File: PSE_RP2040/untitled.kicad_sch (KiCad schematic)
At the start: 28 parts, among them J5 Screw_Terminal_01x02, U7 TPS2375-1, U8 LMR16006YQ

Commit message: modifiche lezione
usb mini,
check s1b
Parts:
- D6: value (none) -> D_Schottky; footprint (none) -> Diode_SMD:D_SMA
- R38, R39: footprint (none) -> Resistor_SMD:R_0603_1608Metric
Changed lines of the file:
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@@
     (property "Reference" "R39" (id 0) (at 102.87 57.15 90))
     (property "Value" "0R NF" (id 1) (at 102.87 59.69 90))
-    (property "Footprint" "" (id 2) (at 102.87 65.278 90)
+    (property "Footprint" "Resistor_SMD:R_0603_1608Metric" (id 2) (at 102.87 65.278 90)
       (effects (font (size 1.27 1.27)) hide)
     )
@@
     (property "Reference" "R38" (id 0) (at 63.5 125.73 90))
     (property "Value" "0R NF" (id 1) (at 63.5 128.27 90))
-    (property "Footprint" "" (id 2) (at 63.5 133.858 90)
+    (property "Footprint" "Resistor_SMD:R_0603_1608Metric" (id 2) (at 63.5 133.858 90)
       (effects (font (size 1.27 1.27)) hide)
     )
@@
       (effects (font (size 1.27 1.27)) (justify left))
     )
-    (property "Value" "" (id 1) (at 200.66 96.2024 90)
-      (effects (font (size 1.27 1.27)) (justify left))
-    )
-    (property "Footprint" "" (id 2) (at 198.12 95.25 0)
-      (effects (font (size 1.27 1.27)) hide)
-    )
+    (property "Value" "D_Schottky" (id 1) (at 200.66 96.2024 90)
+      (effects (font (size 1.27 1.27)) (justify left))
+    )
+    (property "Footprint" "Diode_SMD:D_SMA" (id 2) (at 198.12 95.25 0)
+      (effects (font (size 1.27 1.27)) hide)
+    )

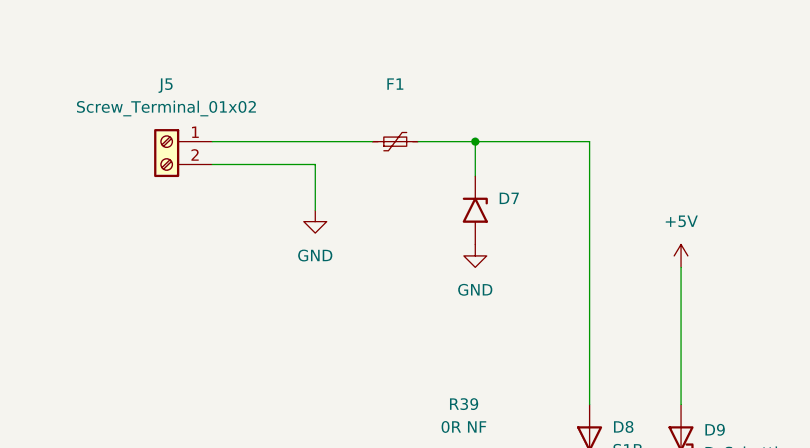
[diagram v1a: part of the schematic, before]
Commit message: footprint
cambiato footprint rp2040 (ora c'è quello con le vias) e footprint tps2375
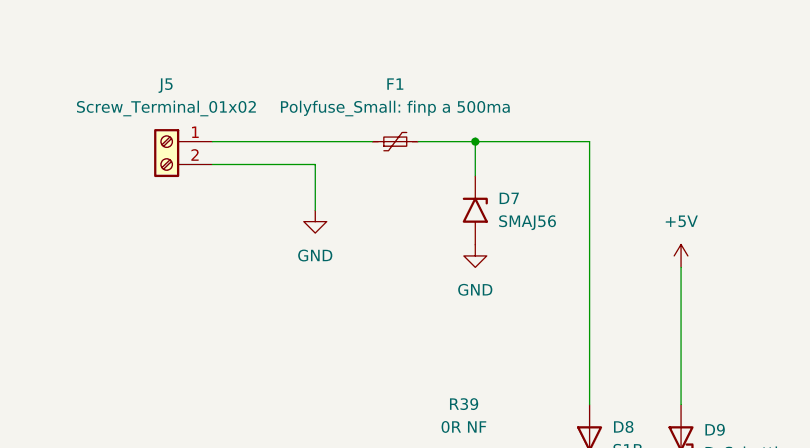
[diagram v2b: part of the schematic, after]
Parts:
- D7: value (none) -> SMAJ56; footprint (none) -> Diode_SMD:D_SMA
- F1: value (none) -> Polyfuse_Small: finp a 500ma; footprint (none) -> Fuse:Fuse_1812_4532Metric
- U7: footprint Package_SO:TSSOP-8_4.4x3mm_P0.65mm -> (none)
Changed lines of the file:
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@@
       (effects (font (size 1.27 1.27)) (justify left))
     )
-    (property "Footprint" "Package_SO:TSSOP-8_4.4x3mm_P0.65mm" (id 2) (at 81.28 111.76 0)
+    (property "Footprint" "" (id 2) (at 81.28 111.76 0)
       (effects (font (size 1.27 1.27)) hide)
     )
@@
     (in_bom yes) (on_board yes) (fields_autoplaced)
     (property "Reference" "F1" (id 0) (at 95.25 21.59 90))
-    (property "Value" "" (id 1) (at 95.25 24.13 90))
-    (property "Footprint" "" (id 2) (at 100.33 26.67 0)
+    (property "Value" "Polyfuse_Small: finp a 500ma" (id 1) (at 95.25 24.13 90))
+    (property "Footprint" "Fuse:Fuse_1812_4532Metric" (id 2) (at 100.33 26.67 0)
       (effects (font (size 1.27 1.27)) (justify left) hide)
     )
@@
       (effects (font (size 1.27 1.27)) (justify left))
     )
-    (property "Value" "" (id 1) (at 106.68 36.8299 90)
-      (effects (font (size 1.27 1.27)) (justify left))
-    )
-    (property "Footprint" "" (id 2) (at 99.06 35.56 0)
-      (effects (font (size 1.27 1.27)) hide)
-    )
+    (property "Value" "SMAJ56" (id 1) (at 106.68 36.8299 90)
+      (effects (font (size 1.27 1.27)) (justify left))
+    )
+    (property "Footprint" "Diode_SMD:D_SMA" (id 2) (at 99.06 35.56 0)
+      (effects (font (size 1.27 1.27)) hide)
+    )

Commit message: allungate pad footprint micro
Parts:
- U7: footprint (none) -> Package_SO:SOIC-8_5.275x5.275mm_P1.27mm
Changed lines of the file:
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@@
       (effects (font (size 1.27 1.27)) (justify left))
     )
-    (property "Footprint" "" (id 2) (at 81.28 111.76 0)
+    (property "Footprint" "Package_SO:SOIC-8_5.275x5.275mm_P1.27mm" (id 2) (at 81.28 111.76 0)
       (effects (font (size 1.27 1.27)) hide)
     )

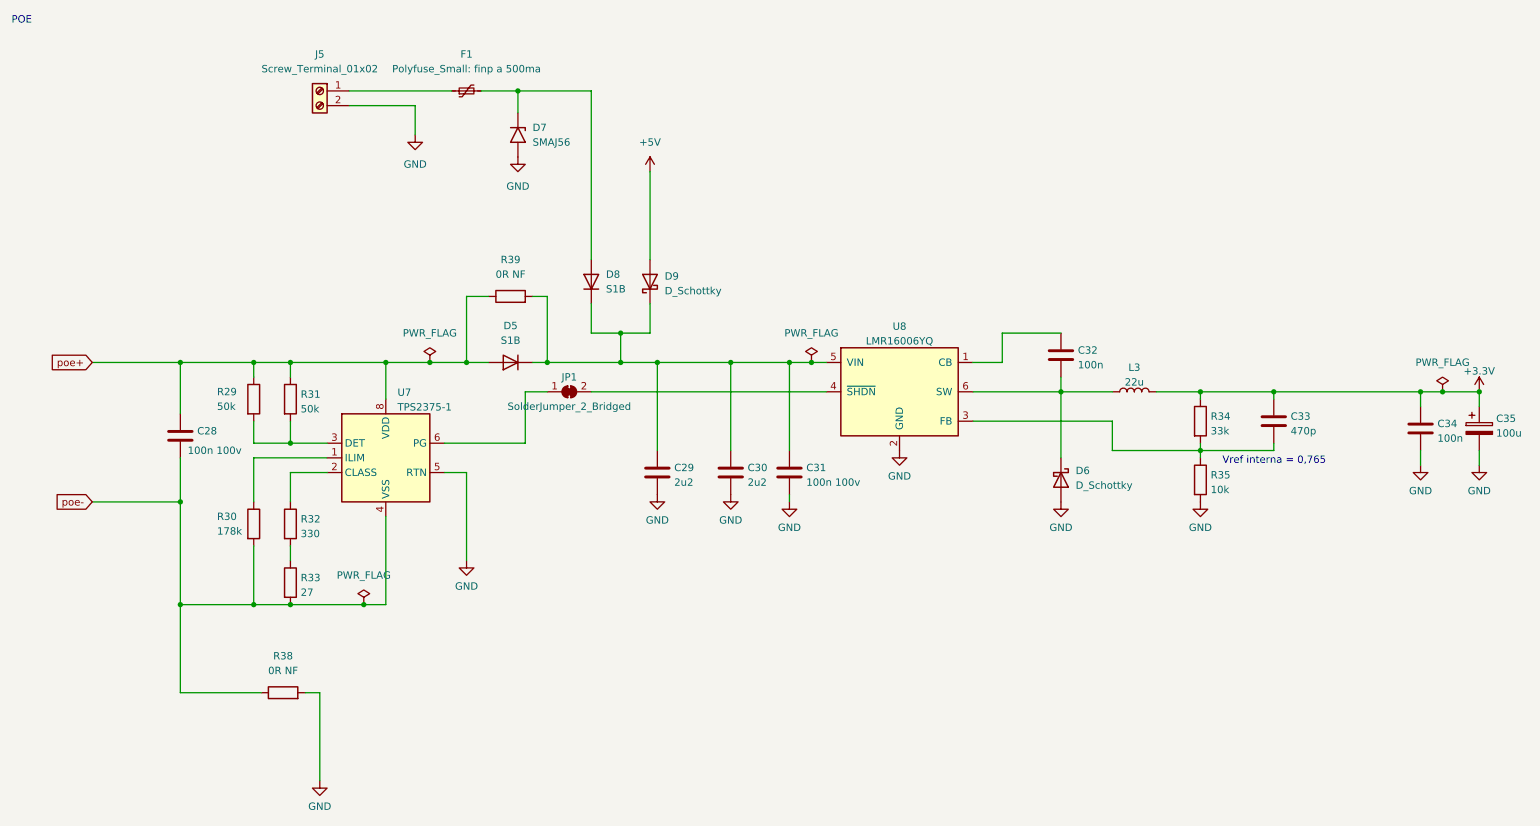
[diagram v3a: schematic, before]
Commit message: check pin, footprint e symb mem
tolto pin 9 al simbolo memoria
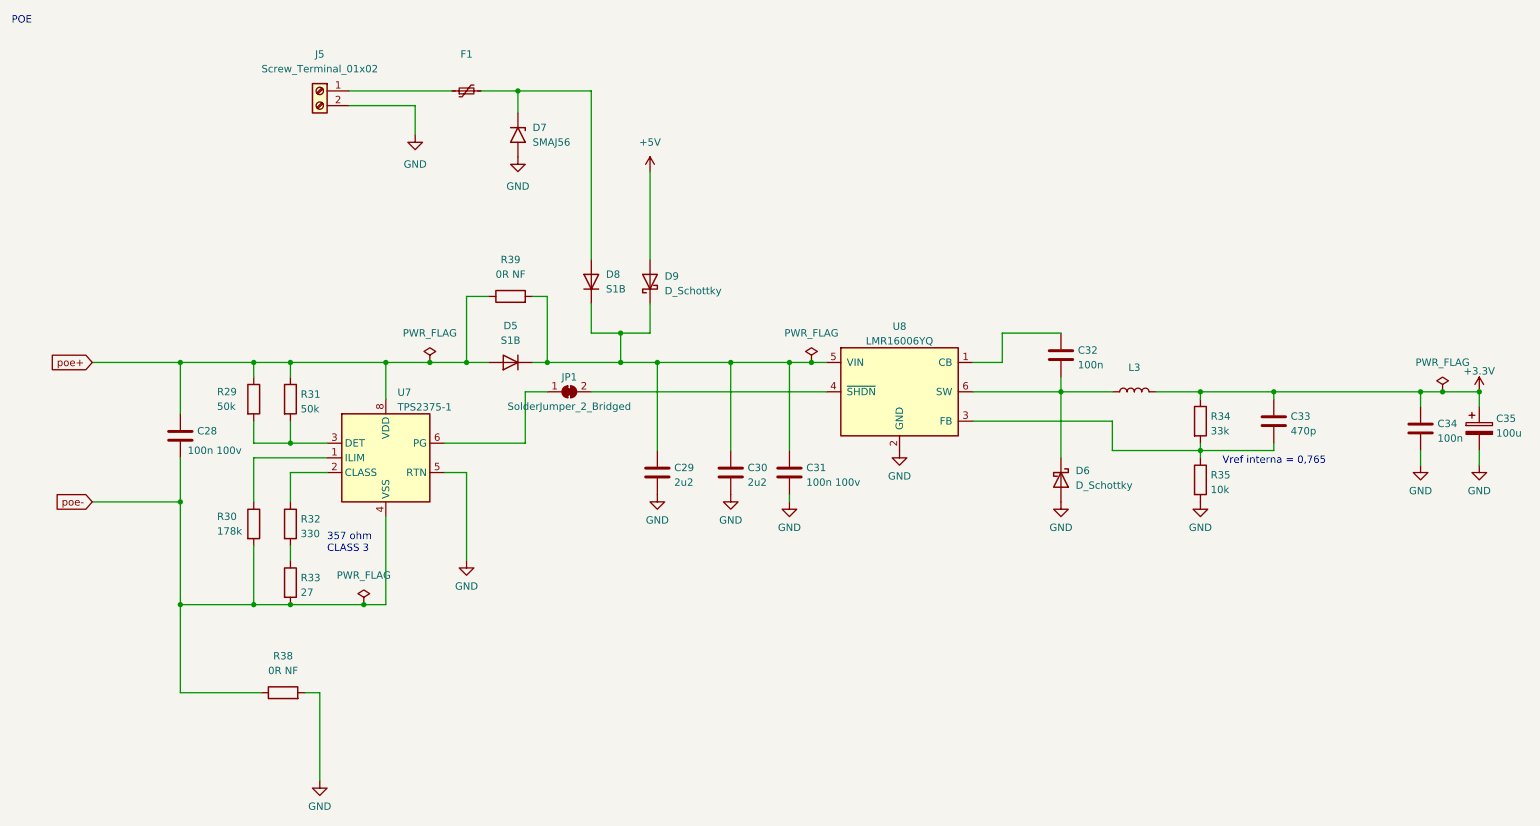
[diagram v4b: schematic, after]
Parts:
- F1: value Polyfuse_Small: finp a 500ma -> (none); footprint Fuse:Fuse_1812_4532Metric -> (none)
- L3: value 22u -> (none); footprint Inductor_SMD:L_6.3x6.3_H3 -> (none)
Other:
- note added: "357 ohm CLASS 3"
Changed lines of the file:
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@@
+    (effects (font (size 1.27 1.27)) (justify left bottom))
+  )
+  (text "357 ohm \nCLASS 3\n" (at 71.12 107.95 0)
     (effects (font (size 1.27 1.27)) (justify left bottom))
   )
@@
     (in_bom yes) (on_board yes) (fields_autoplaced)
     (property "Reference" "F1" (id 0) (at 95.25 21.59 90))
-    (property "Value" "Polyfuse_Small: finp a 500ma" (id 1) (at 95.25 24.13 90))
-    (property "Footprint" "Fuse:Fuse_1812_4532Metric" (id 2) (at 100.33 26.67 0)
+    (property "Value" "" (id 1) (at 95.25 24.13 90))
+    (property "Footprint" "" (id 2) (at 100.33 26.67 0)
       (effects (font (size 1.27 1.27)) (justify left) hide)
     )
@@
     (in_bom yes) (on_board yes) (fields_autoplaced)
     (property "Reference" "L3" (id 0) (at 210.82 75.8022 90))
-    (property "Value" "22u" (id 1) (at 210.82 78.3391 90))
-    (property "Footprint" "Inductor_SMD:L_6.3x6.3_H3" (id 2) (at 210.82 80.01 0)
-      (effects (font (size 1.27 1.27)) hide)
-    )
+    (property "Value" "" (id 1) (at 210.82 78.3391 90))
+    (property "Footprint" "" (id 2) (at 210.82 80.01 0)
+      (effects (font (size 1.27 1.27)) hide)
+    )

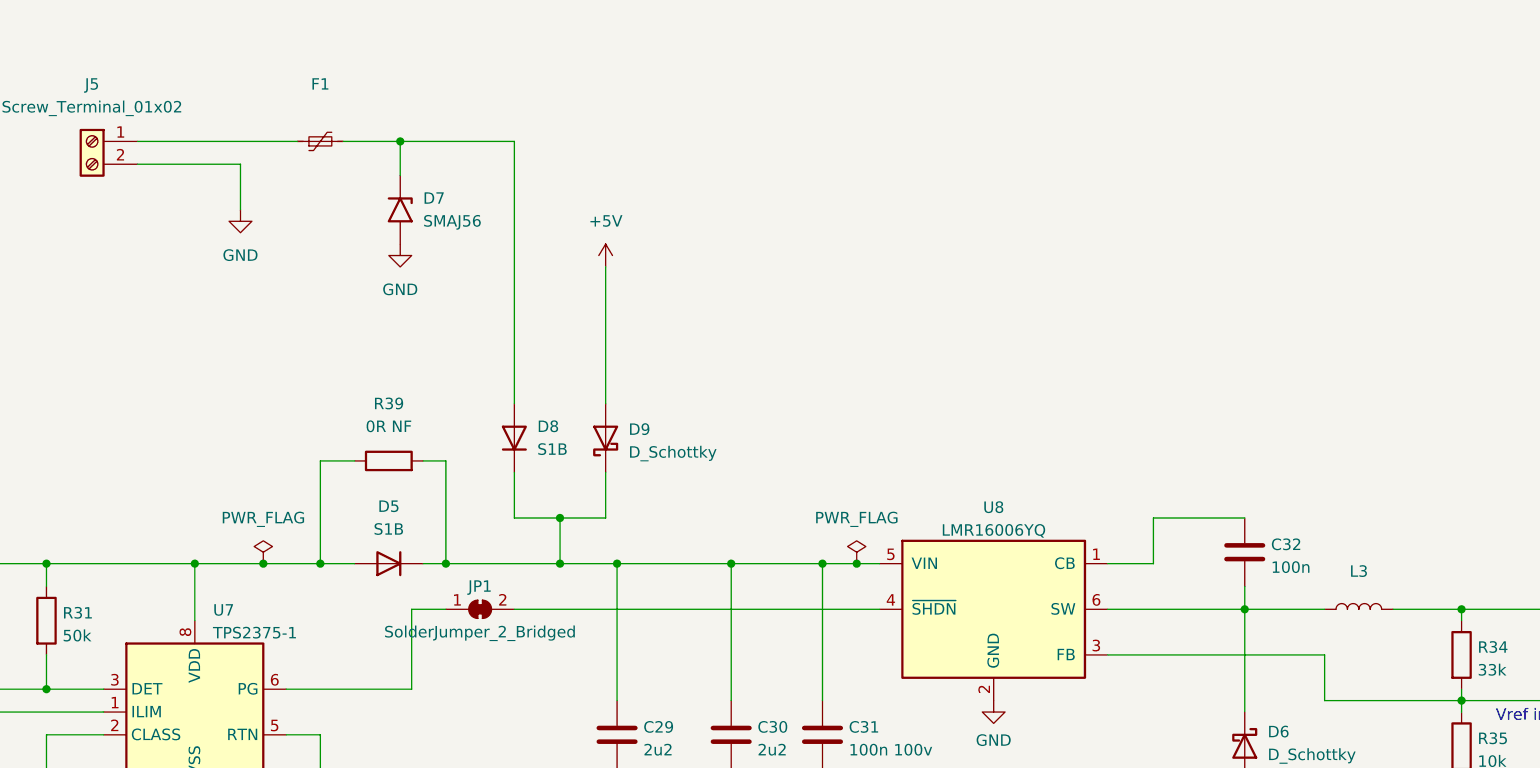
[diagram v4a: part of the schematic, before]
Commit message: piazzamento componenti pcb 1
piazzamento di massima
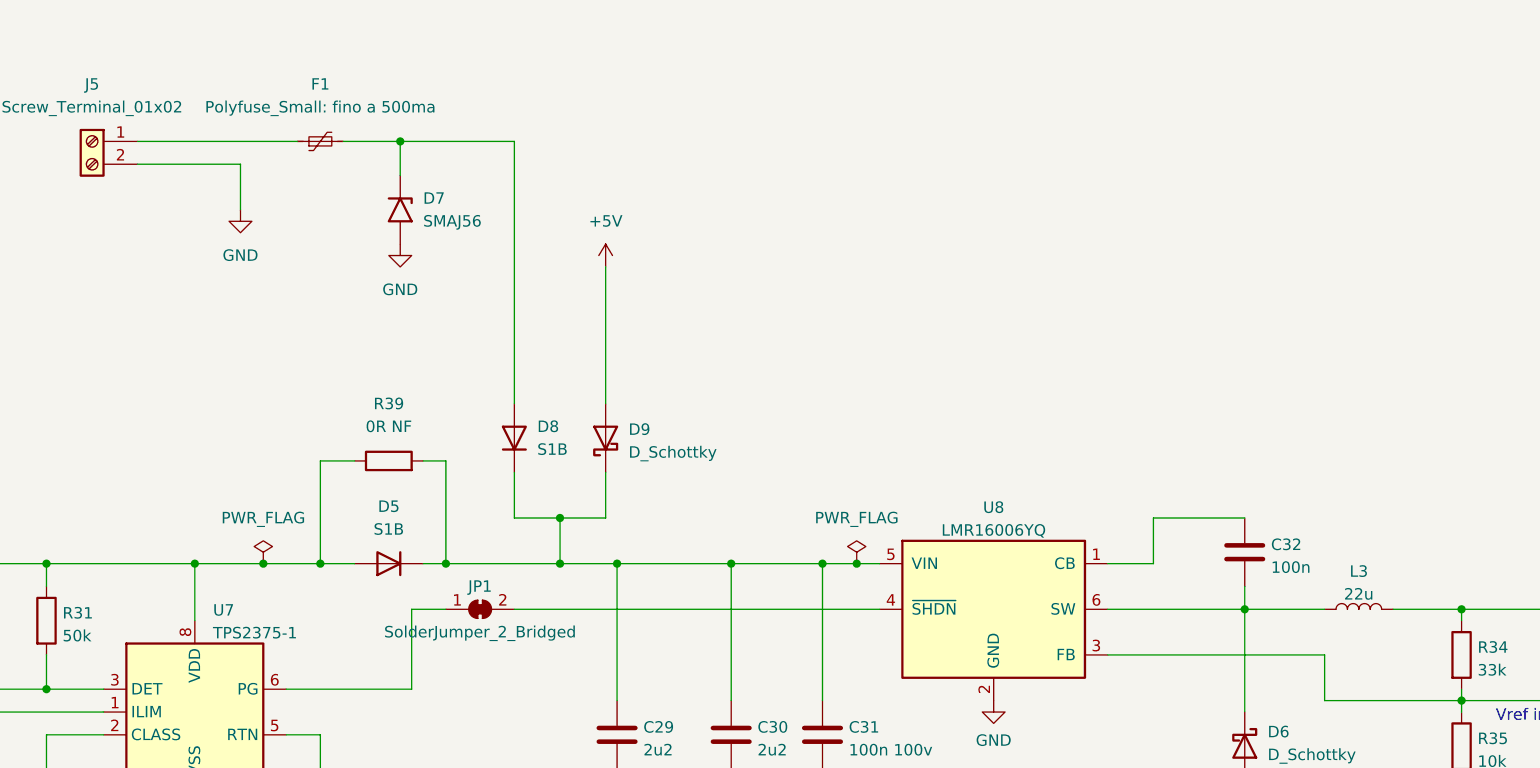
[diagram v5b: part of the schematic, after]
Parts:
- F1: value (none) -> Polyfuse_Small: fino a 500ma; footprint (none) -> Fuse:Fuse_1812_4532Metric
- L3: value (none) -> 22u; footprint (none) -> Inductor_SMD:L_Vishay_IFSC-1515AH_4x4x1.8mm
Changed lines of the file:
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@@
     (in_bom yes) (on_board yes) (fields_autoplaced)
     (property "Reference" "F1" (id 0) (at 95.25 21.59 90))
-    (property "Value" "" (id 1) (at 95.25 24.13 90))
-    (property "Footprint" "" (id 2) (at 100.33 26.67 0)
+    (property "Value" "Polyfuse_Small: fino a 500ma" (id 1) (at 95.25 24.13 90))
+    (property "Footprint" "Fuse:Fuse_1812_4532Metric" (id 2) (at 100.33 26.67 0)
       (effects (font (size 1.27 1.27)) (justify left) hide)
     )
@@
     (in_bom yes) (on_board yes) (fields_autoplaced)
     (property "Reference" "L3" (id 0) (at 210.82 75.8022 90))
-    (property "Value" "" (id 1) (at 210.82 78.3391 90))
-    (property "Footprint" "" (id 2) (at 210.82 80.01 0)
+    (property "Value" "22u" (id 1) (at 210.82 78.3391 90))
+    (property "Footprint" "Inductor_SMD:L_Vishay_IFSC-1515AH_4x4x1.8mm" (id 2) (at 210.82 80.01 0)
       (effects (font (size 1.27 1.27)) hide)
     )

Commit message: pcb merdaccia
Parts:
- C28, C31: value 100n 100v -> (none); footprint Capacitor_SMD:C_0603_1608Metric -> (none)
- C29, C30: value 2u2 -> (none); footprint Capacitor_SMD:C_0603_1608Metric -> (none)
- C32, C34: value 100n -> (none); footprint Capacitor_SMD:C_0603_1608Metric -> (none)
- C33: value 470p -> (none); footprint Capacitor_SMD:C_0603_1608Metric -> (none)
- C35: value 100u -> (none); footprint Capacitor_SMD:C_0805_2012Metric -> (none)
- D5, D8: value S1B -> (none); footprint Diode_SMD:D_SMA -> (none)
- D6, D9: value D_Schottky -> (none); footprint Diode_SMD:D_SMA -> (none)
- D7: value SMAJ56 -> (none); footprint Diode_SMD:D_SMA -> (none)
- F1: value Polyfuse_Small: fino a 500ma -> (none); footprint Fuse:Fuse_1812_4532Metric -> (none)
- J5: value Screw_Terminal_01x02 -> (none); footprint TerminalBlock_Phoenix:TerminalBlock_Phoenix_MKDS-1,5-2-5.08_1x02_P5.08mm_Horizontal -> (none)
- JP1: value SolderJumper_2_Bridged -> (none); footprint Jumper:SolderJumper-2_P1.3mm_Bridged_Pad1.0x1.5mm -> (none)
- L3: value 22u -> (none); footprint Inductor_SMD:L_Vishay_IFSC-1515AH_4x4x1.8mm -> (none)
- R29, R31: value 50k -> (none); footprint Resistor_SMD:R_0603_1608Metric -> (none)
- R30: value 178k -> (none); footprint Resistor_SMD:R_0603_1608Metric -> (none)
- R32: value 330 -> (none); footprint Resistor_SMD:R_0603_1608Metric -> (none)
- R33: value 27 -> (none); footprint Resistor_SMD:R_0603_1608Metric -> (none)
- R34: value 33k -> (none); footprint Resistor_SMD:R_0603_1608Metric -> (none)
- R35: value 10k -> (none); footprint Resistor_SMD:R_0603_1608Metric -> (none)
- R38, R39: value 0R NF -> (none); footprint Resistor_SMD:R_0603_1608Metric -> (none)
- U7: value TPS2375-1 -> (none); footprint Package_SO:SOIC-8_5.275x5.275mm_P1.27mm -> (none)
- U8: value LMR16006YQ -> (none); footprint Package_TO_SOT_SMD:SOT-23-6 -> (none)
